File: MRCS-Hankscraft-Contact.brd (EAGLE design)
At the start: 30.5 x 19.1 mm, 6 parts, among them K2 TN2-4.5V

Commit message: First release sent out to fab
I'll send these to Allison for testing
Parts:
- removed OSHW1: DOC-OSHW-LOGO-M, SPCoast:OSHW-LOGO-M
- moved CON2 1.27 mm to (2.54, 3.81)
- moved SW1 1.27 mm to (21.6, 10.2)
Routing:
- net N$2: track 0.00 -> 34.6 mm
- net N$9: track 0.00 -> 27.5 mm
- net N$6: track 0.00 -> 11.5 mm
- net N$4: track 0.00 -> 9.67 mm
- net N$1: track 0.00 -> 8.93 mm
- net N$3: track 0.00 -> 8.67 mm
- net N$5: track 0.00 -> 7.62 mm
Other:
- board text added: "G +"
- board text added: "O S C O S C"
- board text removed: "Use tPlace/bPlace for silkscreen text and drawings Use Document, tDocu and bDocu for assembly notes and documentation that does NOT go on the board"

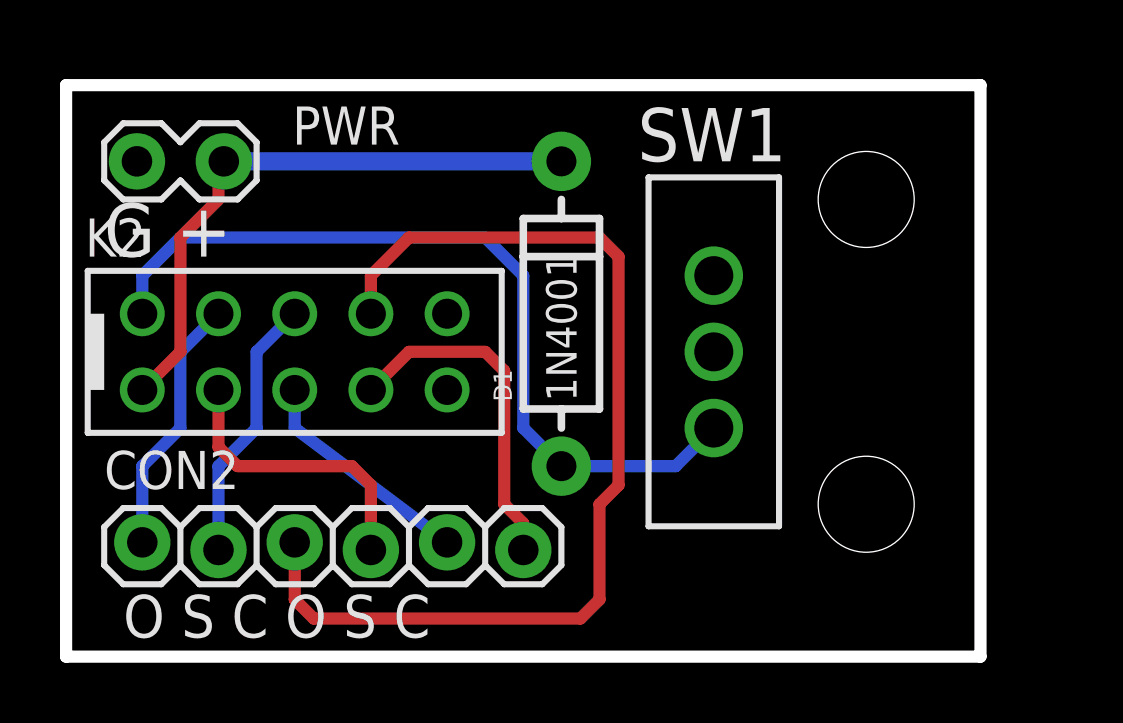
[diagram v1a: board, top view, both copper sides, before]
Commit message: Version 2
changed size to give the uSwitch pads more room, removed footprint for toggle switch, just using test point pads for connections.
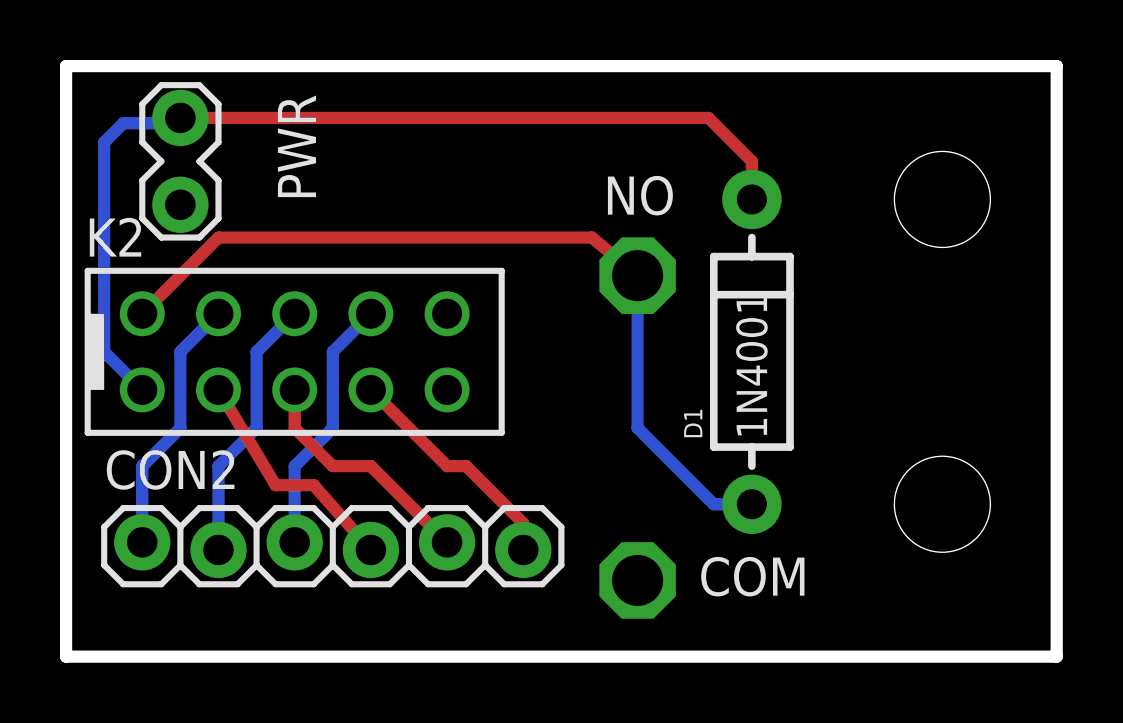
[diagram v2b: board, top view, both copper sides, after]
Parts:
- removed SW1: (no value), SPCoast:SWITCH-SPDT
- added COM, NO: TPPAD1-17, testpad:P1-17
- added U$1: (no value), MRCSLogoTop:MRCSLOGOTOP
- moved D1 6.48 mm to (22.9, 10.2)
- moved PWR 1.80 mm to (3.81, 15.2), turned to 90 degrees
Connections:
- net GND: now also COM.TP; no longer SW1.2
- net N$9: now also NO.TP; no longer SW1.3
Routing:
- net N$2: track 34.6 -> 8.67 mm
- net N$7: track 19.9 -> 32.6 mm
- net N$6: track 11.5 -> 7.81 mm
- net N$4: track 9.67 -> 7.85 mm
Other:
- board size 30.5 x 19.1 mm -> 33 x 19.7 mm
- board text added: "+ G"
- board text added: "2023-01"
- board text added: "COM"
- board text added: "NO"
- board text added: "v1.2"
- board text removed: "2019-11"
- board text removed: "G +"
- board text removed: "v#.#"

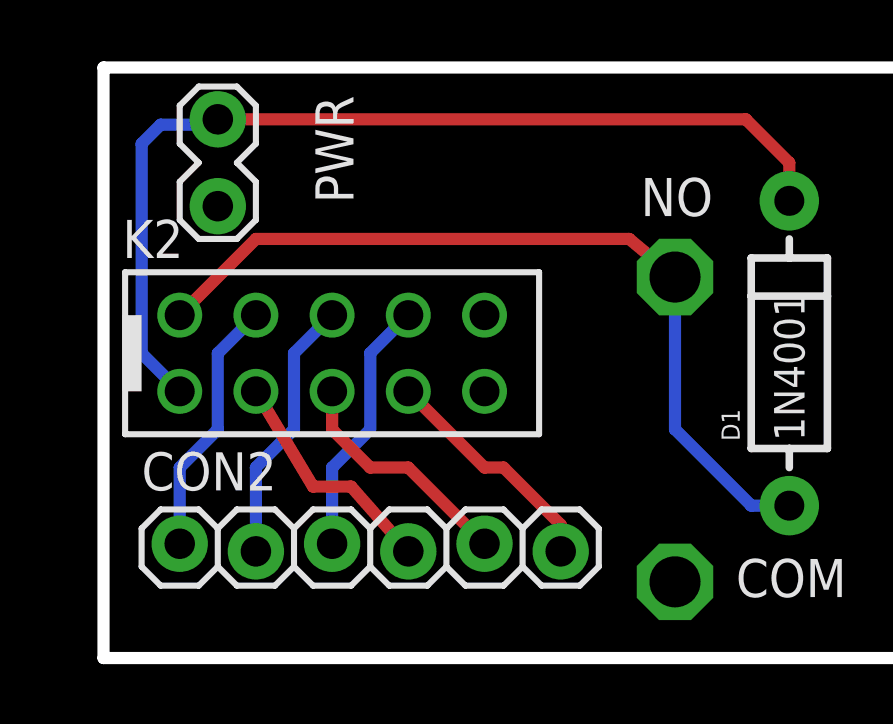
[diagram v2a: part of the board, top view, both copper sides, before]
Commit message: adding back to Github - disappeared
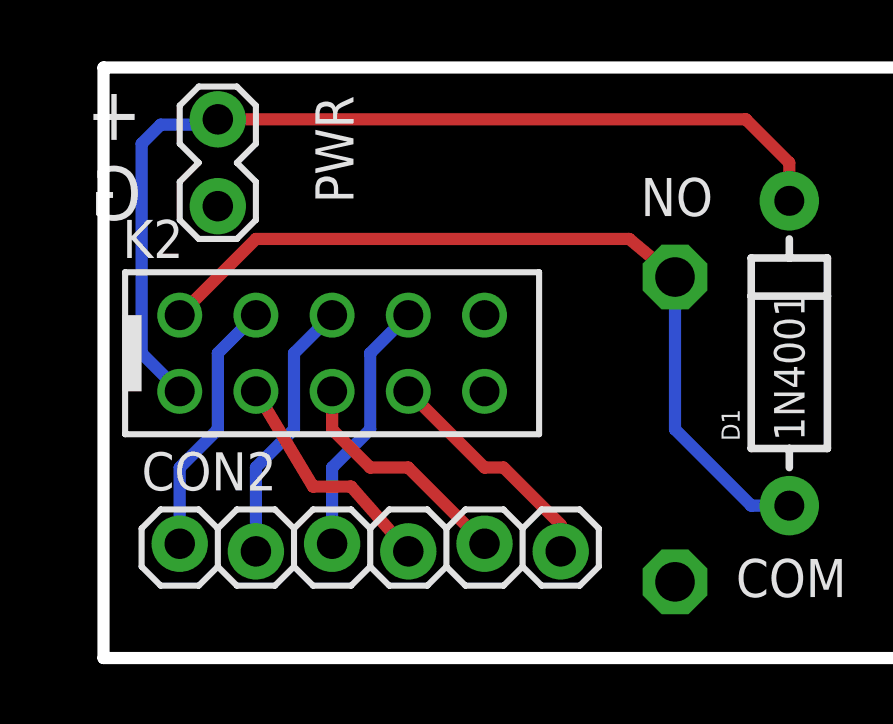
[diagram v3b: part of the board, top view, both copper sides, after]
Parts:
- COM, NO: value TPPAD1-17 -> TPPAD1-13; device testpad:P1-17 -> testpad:P1-13
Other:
- board text added: "2023-02"
- board text added: "C S O C S O"
- board text added: "CON2"
- board text added: "D1"
- board text added: "K2"
- board text added: "PWR"
- board text added: "v1.3"
- board text removed: "2023-01"
- board text removed: "O S C O S C"
- board text removed: "v1.2"
